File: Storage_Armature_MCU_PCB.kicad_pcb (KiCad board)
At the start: 4 copper layers, 163 x 170 mm, 214 parts, among them Q1 20N06, U10 NSI1200, U11 OPA333, U12 NSI1200, U13 OPA333, U14 USBLC6-2P6, U2 NSI1200, U23 RSCD06D3, U24 RSCD06D3, U25 RSCD06D3, U26 RSCD06D3, U3 NSI1200, U4 ADP3338AKCZ-3.3RL7, U5 ADP3338AKCZ-3.3RL7, U6 OPA333, U7 OPA333, U8 NSI1200, U9 OPA333

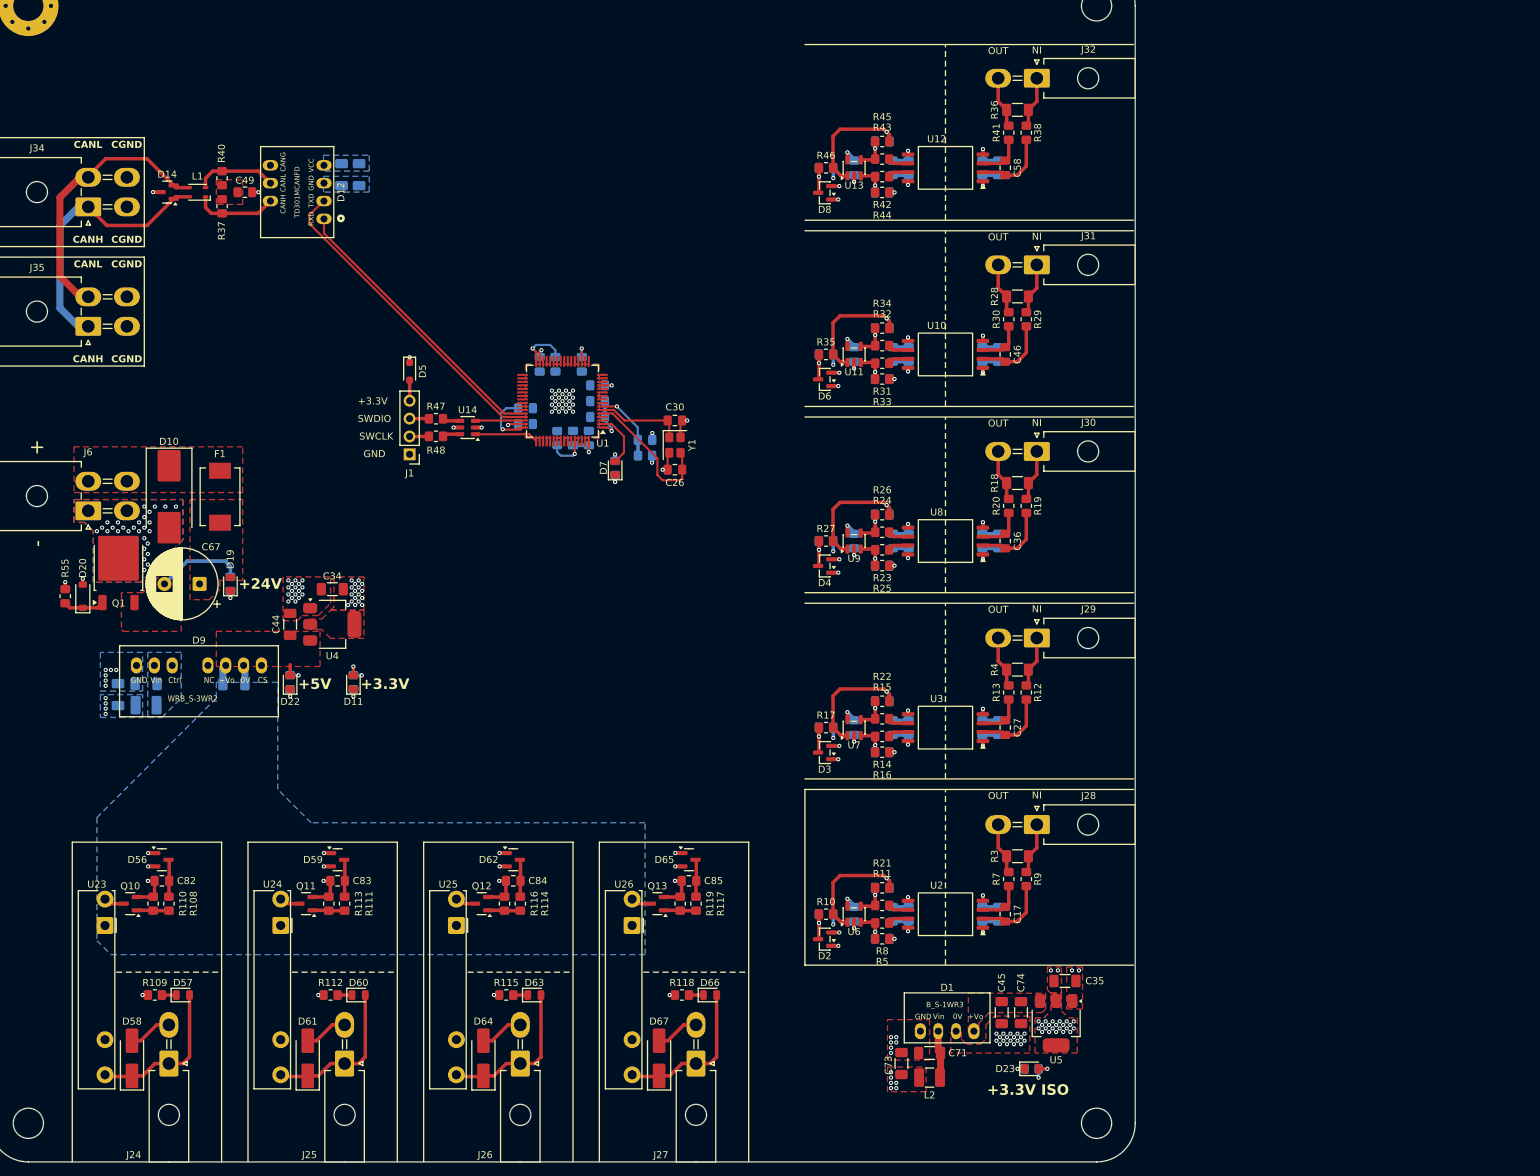
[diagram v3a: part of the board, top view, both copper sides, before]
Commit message: VER1.0: добавил предохранители каждому клапану и отдельно по питанию
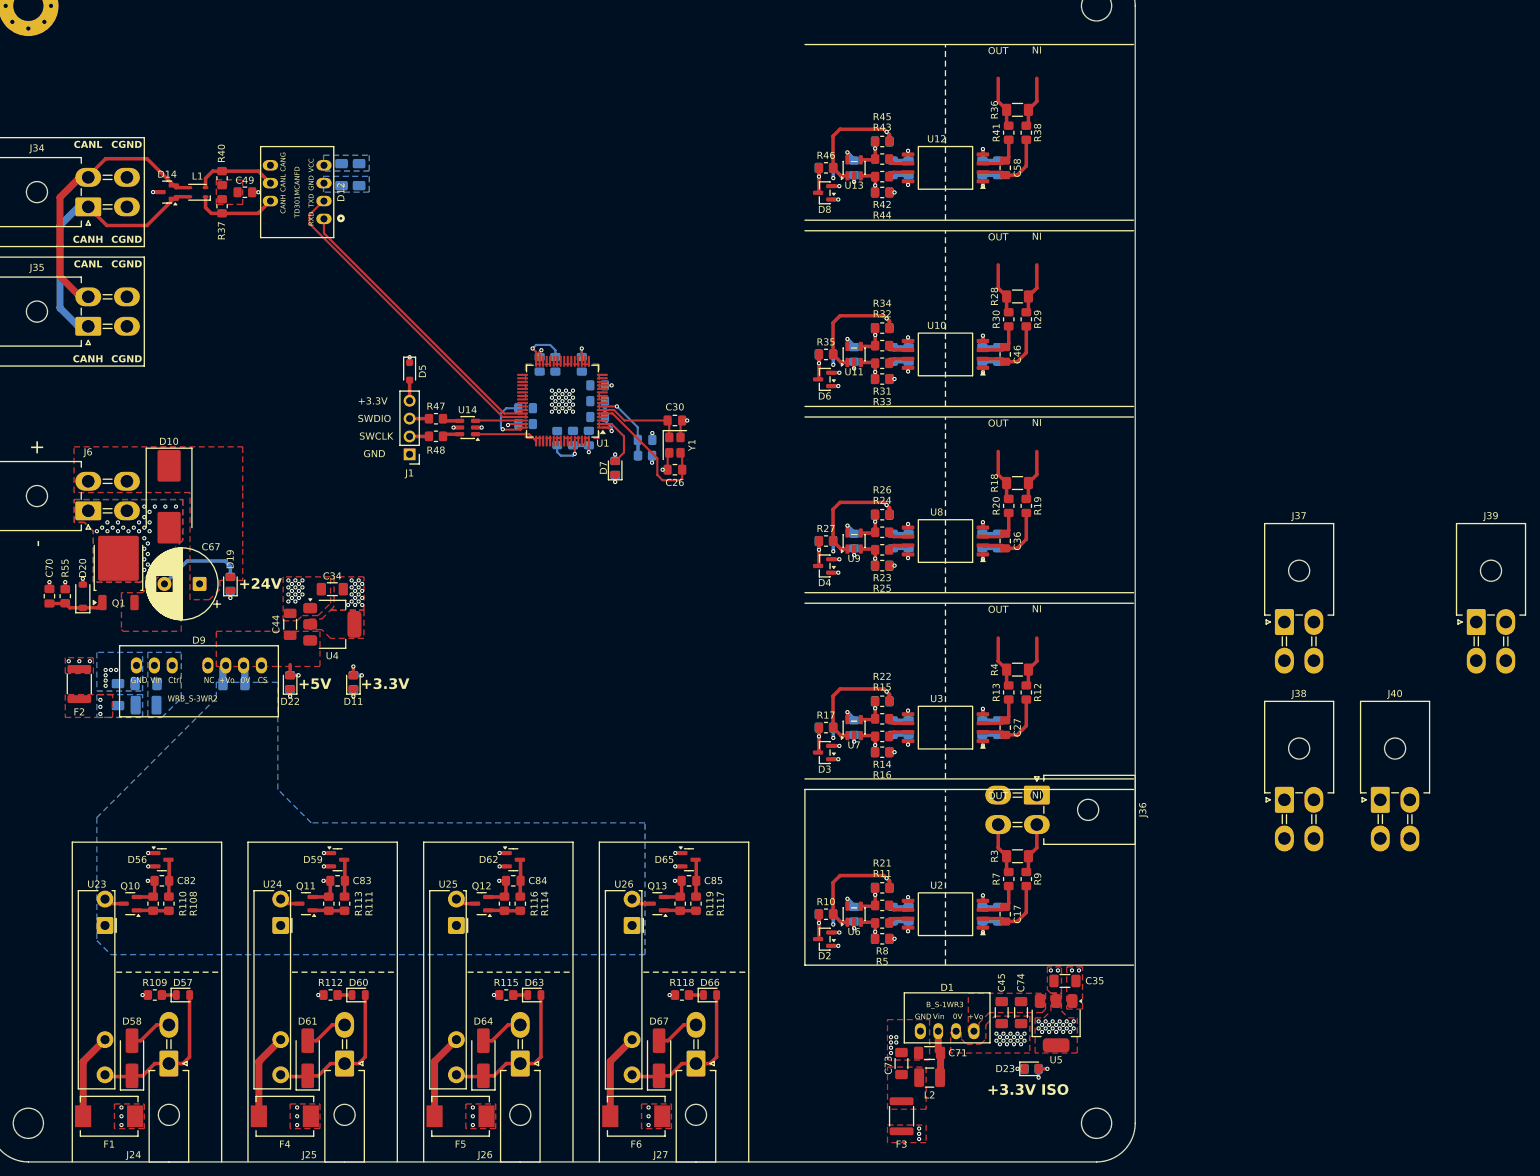
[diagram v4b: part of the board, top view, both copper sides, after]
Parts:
- removed J28, J29, J30, J31, J32: ~, Connector_Molex:Molex_Mini-Fit_Jr_5569-02A2_2x01_P4.20mm_Horizontal
- added C70: 100n, Capacitor_SMD:C_0805_2012Metric_Pad1.18x1.45mm_HandSolder, F.Cu at (228.8, 227.5)
- added F2: MF-MSMF050/30X-2, Fuse:Fuse_1812_4532Metric, F.Cu at (233.0, 240.0)
- added F3: MF-MSMF020, Fuse:Fuse_1812_4532Metric, F.Cu at (350.0, 301.5)
- added F4: MF-SM075/60-2, Fuse:Fuse_Bourns_MF-SM_7.98x5.44mm, F.Cu at (262.2, 301.5)
- added F5: MF-SM075/60-2, Fuse:Fuse_Bourns_MF-SM_7.98x5.44mm, F.Cu at (287.2, 301.5)
- added F6: MF-SM075/60-2, Fuse:Fuse_Bourns_MF-SM_7.98x5.44mm, F.Cu at (312.2, 301.5)
- added J36: ~, Connector_Molex:Molex_Mini-Fit_Jr_5569-04A2_2x02_P4.20mm_Horizontal, F.Cu at (369.2, 255.8)
- added J37: ~, Connector_Molex:Molex_Mini-Fit_Jr_5569-04A2_2x02_P4.20mm_Horizontal, F.Cu at (404.5, 231.2)
- added J38: ~, Connector_Molex:Molex_Mini-Fit_Jr_5569-04A2_2x02_P4.20mm_Horizontal, F.Cu at (404.5, 256.5)
- added J39: ~, Connector_Molex:Molex_Mini-Fit_Jr_5569-04A2_2x02_P4.20mm_Horizontal, F.Cu at (431.8, 231.2)
- added J40: ~, Connector_Molex:Molex_Mini-Fit_Jr_5569-04A2_2x02_P4.20mm_Horizontal, F.Cu at (418.1, 256.5)
- C48: value 0.1u -> 100n
- moved F1 89.6 mm to (237.2, 301.5), turned to 0 degrees
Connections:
- C68 pad 1: +24V -> Net-(C68-Pad1)
- C73 pad 1: +24V -> Net-(C73-Pad1)
- D10 pad 1: +24_IN -> +24V
- F1 pad 1: +24_IN -> Net-(F1-Pad1)
- J6 pad 2: +24_IN -> +24V
- J6 pad 4: +24_IN -> +24V
- L2 pad 1: +24V -> Net-(C73-Pad1)
- L3 pad 1: +24V -> Net-(C68-Pad1)
- U23 pad 11: +24V -> Net-(F1-Pad1)
- U24 pad 11: +24V -> Net-(F4-Pad1)
- U25 pad 11: +24V -> Net-(F5-Pad1)
- U26 pad 11: +24V -> Net-(F6-Pad1)
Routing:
- net Net-(F6-Pad1): track 0.00 -> 12.2 mm
- net Net-(F5-Pad1): track 0.00 -> 12.2 mm
- net Net-(F4-Pad1): track 0.00 -> 12.2 mm
- net Net-(F1-Pad1): track 0.00 -> 12.2 mm
- net Net-(D20-K): track 5.87 -> 8.14 mm
- net GNDD: track 41.1 -> 42.1 mm, vias 17 -> 18
- net Net-(C68-Pad1): vias 0 -> 3
- net +24V: vias 11 -> 19
- added copper zone on F.Cu, net Net-(C68-Pad1)
- added copper zone on F.Cu, net Net-(C73-Pad1)
- removed copper zone on F.Cu, net +24_IN

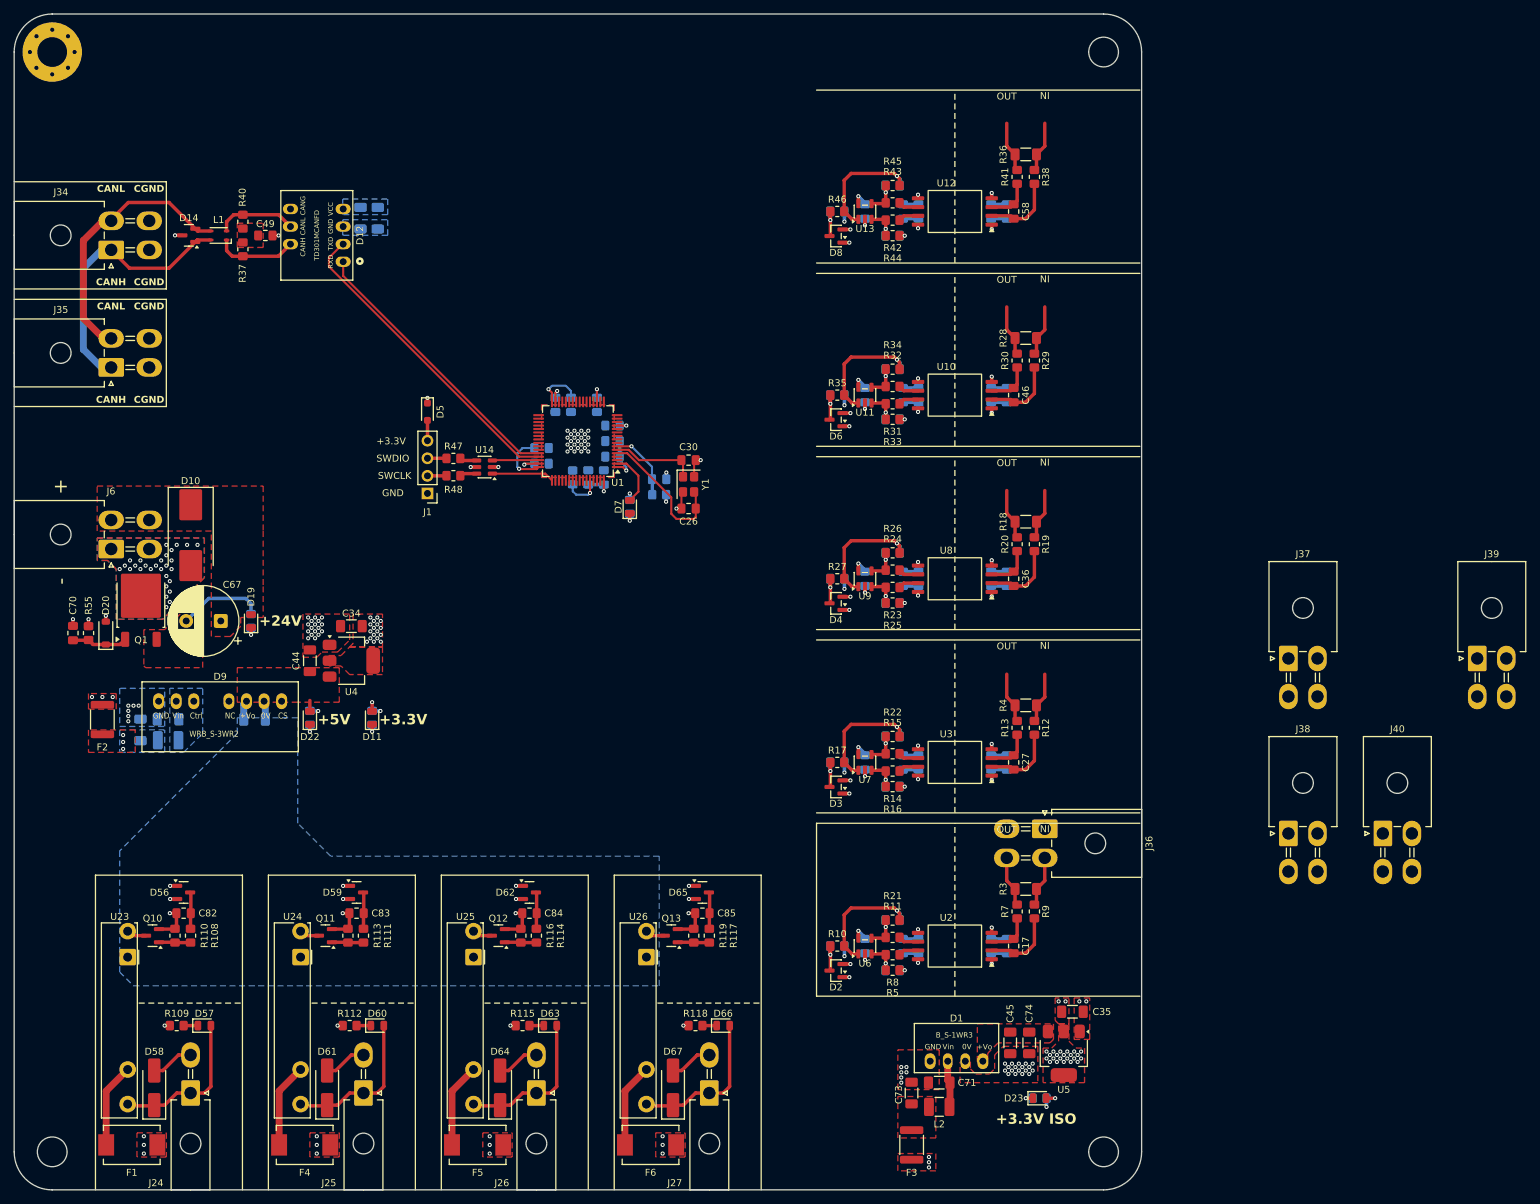
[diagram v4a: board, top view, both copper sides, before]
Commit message: VER1.0: объединил земли датчиков и 24В
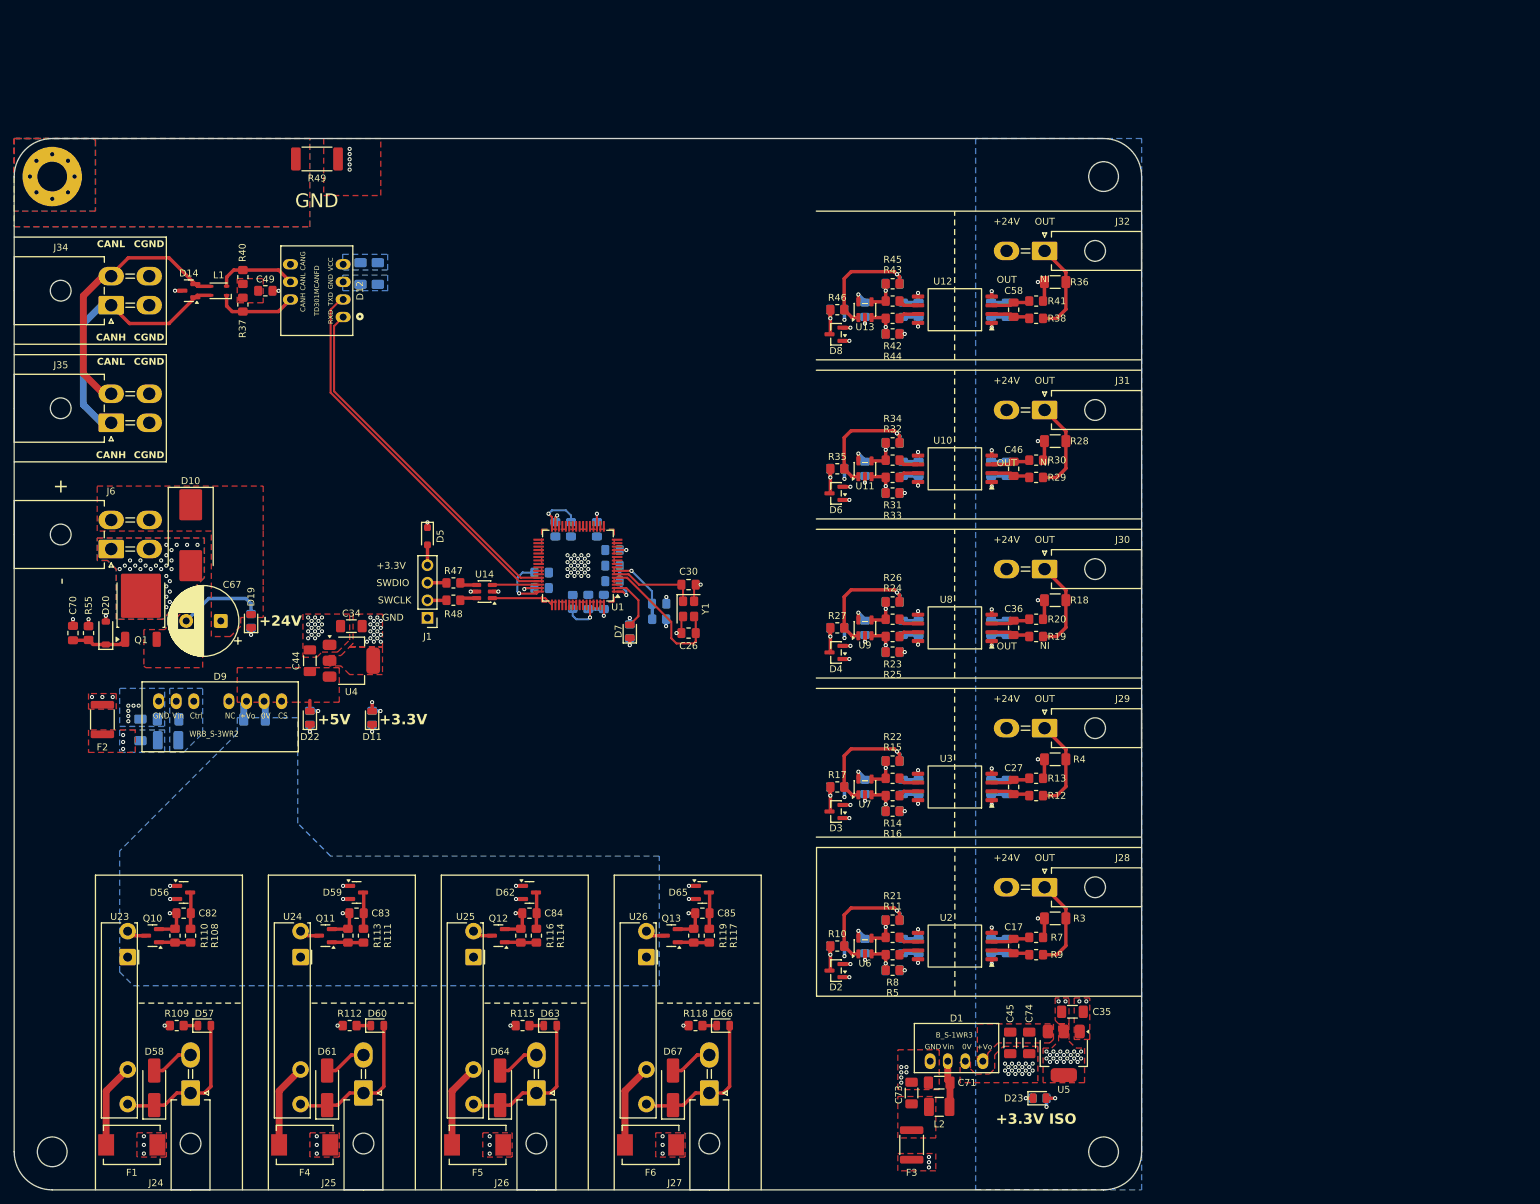
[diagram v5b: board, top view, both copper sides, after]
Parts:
- removed J36, J37, J38, J39, J40: ~, Connector_Molex:Molex_Mini-Fit_Jr_5569-04A2_2x02_P4.20mm_Horizontal
- added J28: ~, Connector_Molex:Molex_Mini-Fit_Jr_5569-02A2_2x01_P4.20mm_Horizontal, F.Cu at (369.2, 264.2)
- added J29: ~, Connector_Molex:Molex_Mini-Fit_Jr_5569-02A2_2x01_P4.20mm_Horizontal, F.Cu at (369.2, 241.2)
- added J30: ~, Connector_Molex:Molex_Mini-Fit_Jr_5569-02A2_2x01_P4.20mm_Horizontal, F.Cu at (369.2, 218.2)
- added J31: ~, Connector_Molex:Molex_Mini-Fit_Jr_5569-02A2_2x01_P4.20mm_Horizontal, F.Cu at (369.2, 195.2)
- added J32: ~, Connector_Molex:Molex_Mini-Fit_Jr_5569-02A2_2x01_P4.20mm_Horizontal, F.Cu at (369.2, 172.2)
- added R49: 0, Resistor_SMD:R_2512_6332Metric_Pad1.40x3.35mm_HandSolder, F.Cu at (264.0, 159.0)
- moved R38 20.5 mm to (368.0, 182.0), turned to 180 degrees
- moved R36 18.9 mm to (370.8, 176.8)
- moved R41 18.2 mm to (368.0, 179.5), turned to 180 degrees
- moved C1 18.0 mm to (305.5, 223.0)
- moved C12 18.0 mm to (304.5, 212.5)
- moved C13 18.0 mm to (303.2, 223.0)
- moved C14 18.0 mm to (306.8, 220.0)
- moved C15 18.0 mm to (306.8, 217.8)
- moved C2 18.0 mm to (300.8, 212.5)
- moved C20 18.0 mm to (298.5, 212.5)
- moved C21 18.0 mm to (296.5, 221.0)
- moved C26 18.0 mm to (317.8, 227.5)
- moved C30 18.0 mm to (317.8, 220.5)
- moved C65 18.0 mm to (313.5, 223.2)
- moved C8 18.0 mm to (296.5, 218.8)
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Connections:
- net /Sensor_1/P_IN renamed Net-(J28-Pin_1)
- net /Sensor_2/P_IN renamed Net-(J29-Pin_1)
- net /Sensor_3/P_IN renamed Net-(J30-Pin_1)
- net /Sensor_4/P_IN renamed Net-(J31-Pin_1)
- net /Sensor_5/P_IN renamed Net-(J32-Pin_1)
- C18 pad 2: GND_ISO -> GNDD
- C19 pad 2: GND_ISO -> GNDD
- C24 pad 2: GND_ISO -> GNDD
- C25 pad 2: GND_ISO -> GNDD
- C32 pad 2: GND_ISO -> GNDD
- C33 pad 2: GND_ISO -> GNDD
- C35 pad 1: GND_ISO -> GNDD
- C42 pad 2: GND_ISO -> GNDD
- C43 pad 2: GND_ISO -> GNDD
- C45 pad 1: GND_ISO -> GNDD
- C56 pad 2: GND_ISO -> GNDD
- C57 pad 2: GND_ISO -> GNDD
- C74 pad 2: GND_ISO -> GNDD
- D1 pad 3: GND_ISO -> GNDD
- R13 pad 1: /Sensor_2/P_OUT -> GNDD
- R18 pad 2: /Sensor_3/P_OUT -> GNDD
- R20 pad 1: /Sensor_3/P_OUT -> GNDD
- R28 pad 2: /Sensor_4/P_OUT -> GNDD
- R3 pad 2: /Sensor_1/P_OUT -> GNDD
- R30 pad 1: /Sensor_4/P_OUT -> GNDD
- R36 pad 2: /Sensor_5/P_OUT -> GNDD
- R4 pad 2: /Sensor_2/P_OUT -> GNDD
- R41 pad 1: /Sensor_5/P_OUT -> GNDD
- R58 pad 2: GND_ISO -> GNDD
- R7 pad 1: /Sensor_1/P_OUT -> GNDD
- U10 pad 4: GND_ISO -> GNDD
- U12 pad 4: GND_ISO -> GNDD
- U2 pad 4: GND_ISO -> GNDD
- U3 pad 4: GND_ISO -> GNDD
- U5 pad 1: GND_ISO -> GNDD
- U8 pad 4: GND_ISO -> GNDD
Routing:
- net GNDD: track 42.1 -> 85.7 mm, vias 18 -> 49
- net GND_ISO: track 24.7 -> 0.00 mm, vias 26 -> 0
- net /CAN_RXD_MCU: track 40.9 -> 52.0 mm
- net /CAN_TXD_MCU: track 45.8 -> 55.8 mm
- net /Sensor_4/P_OUT: track 7.37 -> 0.00 mm
- net /Sensor_2/P_OUT: track 7.37 -> 0.00 mm
- net /Sensor_1/P_OUT: track 7.37 -> 0.00 mm
- net /Sensor_3/P_OUT: track 7.37 -> 0.00 mm
- net /Sensor_5/P_OUT: track 7.37 -> 0.00 mm
- net Net-(J32-Pin_1): track 7.37 -> 13.6 mm
- net Net-(J30-Pin_1): track 7.37 -> 13.6 mm
- net Net-(J28-Pin_1): track 7.37 -> 13.6 mm
- net Net-(J31-Pin_1): track 7.37 -> 13.6 mm
- net Net-(J29-Pin_1): track 7.37 -> 13.6 mm
- net Net-(C17-Pad1): track 10.1 -> 5.11 mm
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- added copper zone on B.Cu, net +3.3V_ISO
- added copper zone on In2.Cu, net GND
- removed copper zone on In2.Cu, net +3.3V_ISO
- removed copper zone on F.Cu, net GND_ISO
- removed copper zone on In1.Cu, net GND_ISO
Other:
- board size 163 x 170 mm -> 163 x 152 mm
